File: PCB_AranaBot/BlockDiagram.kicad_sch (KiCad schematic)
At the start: 0 parts

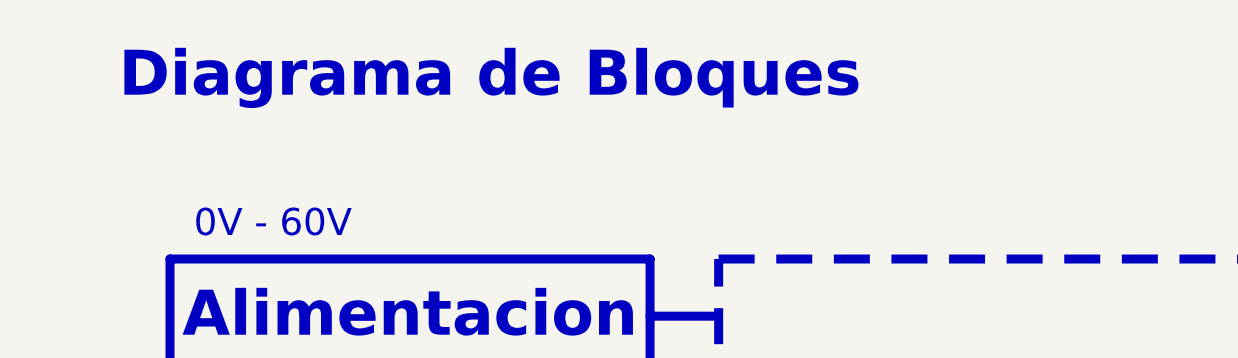
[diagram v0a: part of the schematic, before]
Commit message: Update 3
Se realizó la configuración inicial del MCU, capacitores de desacople, reloj externo, y Ferrite Bread para reducir el EMI, labels con cada función de los GPIOS
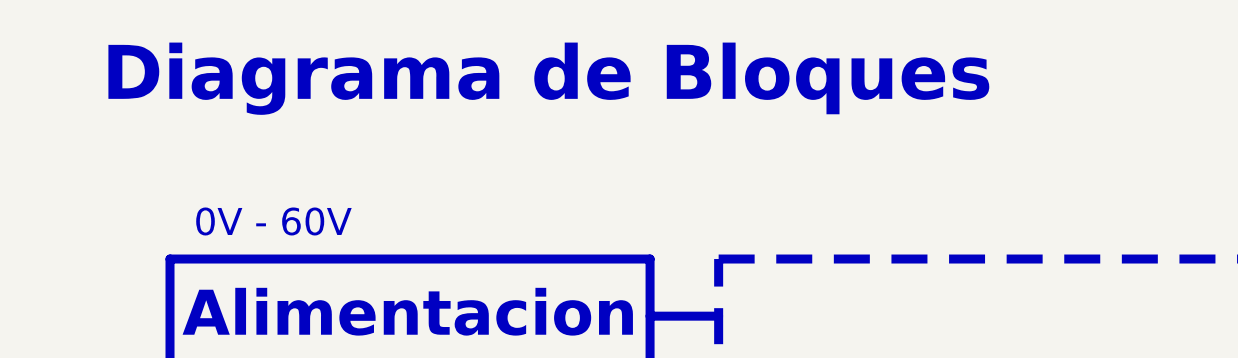
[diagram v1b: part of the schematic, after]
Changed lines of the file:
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@@
 	(text "Diagrama de Bloques"
 		(exclude_from_sim no)
-		(at 57.15 20.32 0)
+		(at 63.5 20.32 0)
 		(effects
 			(font
-				(size 5 5)
-				(thickness 1)
+				(size 6 6)
+				(thickness 1.2)
 				(bold yes)
 			)
